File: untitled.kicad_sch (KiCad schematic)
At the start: 41 parts, among them J15 Brake/FwRev, J16 5v_in, J17 3.3v_in, J18 12v_in, J2 Raspberry_Pi_4, J21 CAN, J23 5v_rail, J24 3.3v_rail, J25 12v_rail, J26 GND_rail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

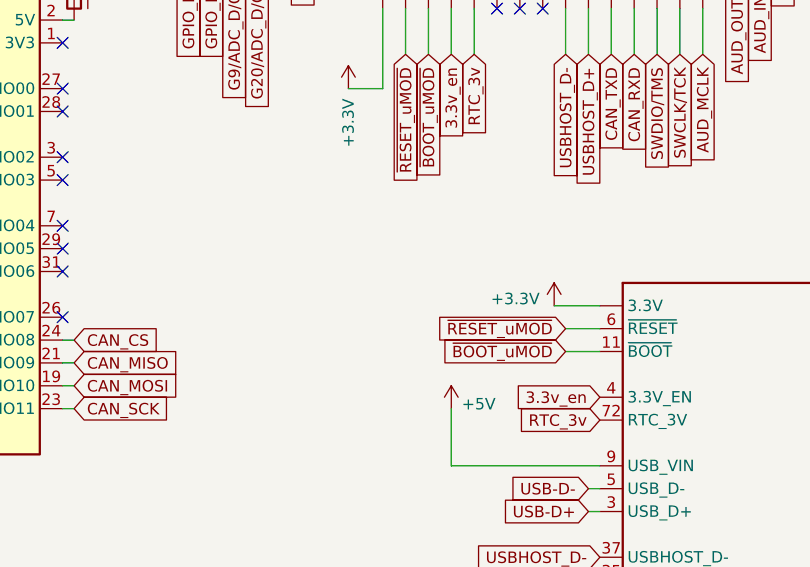
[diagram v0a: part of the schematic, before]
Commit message: fix level shifting in schematic
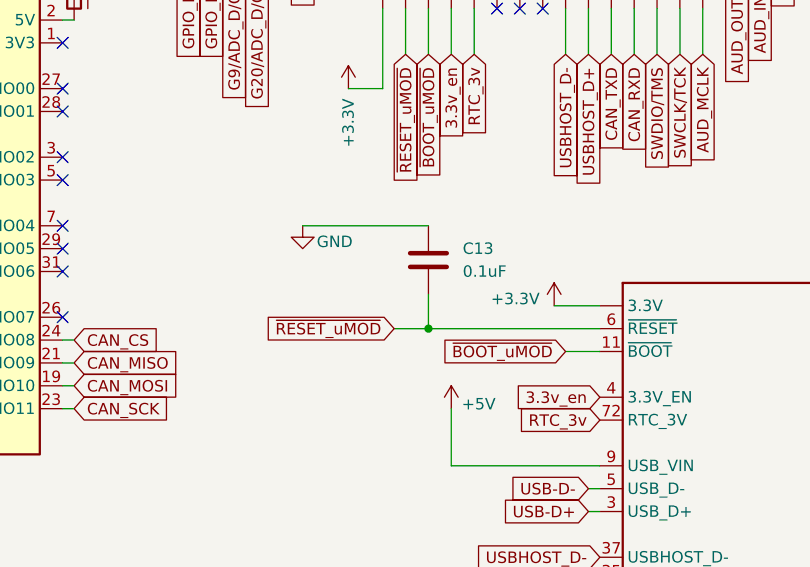
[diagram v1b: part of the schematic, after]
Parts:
- added C13: 0.1uF, Capacitor_SMD:C_1206_3216Metric, symbol Device:C
- J19: footprint SparkFun-Connectors:JST-2-PTH -> Connector_JST:JST_XA_B02B-XASK-1-A_1x02_P2.50mm_Vertical
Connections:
- net GND: now also C13.1
- net ~{RESET_uMOD}: now also C13.2
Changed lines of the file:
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@@
 	)
 	(junction
+		(at 180.34 69.85)
+		(diameter 0)
+		(color 0 0 0 0)
+	)
+	(junction
 		(at 21.59 110.49)
 		(diameter 0)
@@
 	(wire
 		(pts
+			(xy 180.34 69.85) (xy 176.53 69.85)
+		)
+		(stroke
+			(width 0)
+			(type default)
+		)
+	)
+	(wire
+		(pts
 			(xy 43.18 92.71) (xy 43.18 88.9)
 		)
@@
 	(wire
 		(pts
+			(xy 166.37 58.42) (xy 180.34 58.42)
+		)
+		(stroke
+			(width 0)
+			(type default)
+		)
+	)
+	(wire
+		(pts
 			(xy 185.42 16.51) (xy 185.42 21.59)
 		)
@@
 	(wire
 		(pts
-			(xy 199.39 69.85) (xy 195.58 69.85)
+			(xy 199.39 69.85) (xy 180.34 69.85)
 		)
 		(stroke
@@
 	(wire
 		(pts
+			(xy 180.34 66.04) (xy 180.34 69.85)
+		)
+		(stroke
+			(width 0)
+			(type default)
+		)
+	)
+	(wire
+		(pts
 			(xy 125.73 193.04) (xy 125.73 181.61)
 		)
@@
 	(global_label "~{RESET_uMOD}"
 		(shape input)
-		(at 195.58 69.85 180)
+		(at 176.53 69.85 180)
 		(fields_autoplaced yes)
 		(effects
@@
 		)
 		(property "Intersheetrefs" "${INTERSHEET_REFS}"
-			(at 180.6812 69.85 0)
+			(at 161.6312 69.85 0)
 			(effects
 				(font
@@
 			)
 		)
-		(property "Footprint" "SparkFun-Connectors:JST-2-PTH"
+		(property "Footprint" "Connector_JST:JST_XA_B02B-XASK-1-A_1x02_P2.50mm_Vertical"
 			(at 92.71 180.34 0)
 			(effects
@@
 					(unit 1)
 				)
+			)
+		)
+	)
+	(symbol
+		(lib_id "power:GND")
+		(at 166.37 58.42 0)
+		(unit 1)
+		(exclude_from_sim no)
+		(in_bom yes)
+		(on_board yes)
+		(dnp no)
+		(property "Reference" "#PWR051"
+			(at 166.37 64.77 0)
+			(effects
+				(font
+					(size 1.27 1.27)
+				)
+				(hide yes)
+			)
+		)
+		(property "Value" "GND"
+			(at 169.926 60.198 0)
+			(effects
+				(font
+					(size 1.27 1.27)
+				)
+			)
+		)
+		(property "Footprint" ""
+			(at 166.37 58.42 0)
+			(effects
+				(font
+					(size 1.27 1.27)
+				)
+				(hide yes)
+			)
+		)
+		(property "Datasheet" ""
+			(at 166.37 58.42 0)
+			(effects
+				(font
+					(size 1.27 1.27)
+				)
+				(hide yes)
+			)
+		)
+		(property "Description" "Power symbol creates a global label with name \"GND\" , ground"
+			(at 166.37 58.42 0)
+			(effects
+				(font
+					(size 1.27 1.27)
+				)
+				(hide yes)
+			)
+		)
+		(pin "1"
+		)
+		(instances
+			(project "AAV_embedded"
+				(path "/00c590f3-503a-497c-946e-4acf8f8302df/c057d648-8c01-4f47-9aa9-79a3508e8159"
+					(reference "#PWR051")
+					(unit 1)
+				)
+			)
+		)
+	)
+	(symbol
+		(lib_id "Device:C")
+		(at 180.34 62.23 0)
+		(unit 1)
+		(exclude_from_sim no)
+		(in_bom yes)
+		(on_board yes)
+		(dnp no)
+		(fields_autoplaced yes)
+		(property "Reference" "C13"
+			(at 184.15 60.9599 0)
+			(effects
+				(font
+					(size 1.27 1.27)
+				)
+				(justify left)
+			)
+		)
+		(property "Value" "0.1uF"
+			(at 184.15 63.4999 0)
+			(effects
+				(font
+					(size 1.27 1.27)
+				)
+				(justify left)
+			)
+		)
+		(property "Footprint" "Capacitor_SMD:C_1206_3216Metric"
+			(at 181.3052 66.04 0)
+			(effects
+				(font
+					(size 1.27 1.27)
+				)
+				(hide yes)
+			)
+		)
+		(property "Datasheet" "~"
+			(at 180.34 62.23 0)
+			(effects
+				(font
+					(size 1.27 1.27)
+				)
+				(hide yes)
+			)
+		)
+		(property "Description" "Unpolarized capacitor"
+			(at 180.34 62.23 0)
+			(effects
+				(font
+					(size 1.27 1.27)
+				)
+				(hide yes)
+			)
+		)
+		(pin "2"
+		)
+		(pin "1"
+		)
+		(instances
+			(project "AAV_embedded"
+				(path "/00c590f3-503a-497c-946e-4acf8f8302df/c057d648-8c01-4f47-9aa9-79a3508e8159"
+					(reference "C13")
+					(unit 1)
+				)
